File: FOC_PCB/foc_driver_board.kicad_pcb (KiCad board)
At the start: 4 copper layers, 98 x 63.4 mm, 49 parts, among them J1 STM32-Prog-Header, J2 Conn_01x02_Pin, J3 Conn_01x06_Pin, J4 Conn_01x18, J5 Conn_01x02_Pin, SW1 SW_Push, U2 AZ1117IH-3.3, U3 AZ1117IH-5.0, U4 MCP2542FD, U5 STM32G491KEUx, U6 MCP6007, X1 OXETDLJANF-8MHZ

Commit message: Refactor PCB layout
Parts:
- removed C9: 0u1, Capacitor_SMD:C_0603_1608Metric
- removed J5: Conn_01x02_Pin, Connector_PinSocket_2.54mm:PinSocket_1x02_P2.54mm_Vertical
- removed R2: 10k, Resistor_SMD:R_0603_1608Metric
- removed SW1: SW_Push, Button_Switch_THT:SW_PUSH_6mm
- removed U5: STM32G491KEUx, Package_DFN_QFN:QFN-32-1EP_5x5mm_P0.5mm_EP3.45x3.45mm
- added C20: 0u1, Capacitor_SMD:C_0603_1608Metric_Pad1.08x0.95mm_HandSolder, B.Cu at (166.5, 88.5)
- added C21: 0u1, Capacitor_SMD:C_0603_1608Metric_Pad1.08x0.95mm_HandSolder, B.Cu at (165.5, 92.1)
- added C22: 0u1, Capacitor_SMD:C_0603_1608Metric_Pad1.08x0.95mm_HandSolder, B.Cu at (161.0, 92.1)
- added C23: 1u, Capacitor_SMD:C_0603_1608Metric_Pad1.08x0.95mm_HandSolder, B.Cu at (162.5, 92.1)
- added C24: 0u1, Capacitor_SMD:C_0603_1608Metric_Pad1.08x0.95mm_HandSolder, F.Cu at (194.0, 92.5)
- added C25: 0u1, Capacitor_SMD:C_0603_1608Metric_Pad1.08x0.95mm_HandSolder, F.Cu at (194.0, 89.0)
- added C28: 0u1, Capacitor_SMD:C_0603_1608Metric_Pad1.08x0.95mm_HandSolder, B.Cu at (162.2, 78.0)
- added C29: 0u1, Capacitor_SMD:C_0603_1608Metric_Pad1.08x0.95mm_HandSolder, B.Cu at (172.0, 78.0)
- added C30: 0u1, Capacitor_SMD:C_0603_1608Metric_Pad1.08x0.95mm_HandSolder, B.Cu at (179.2, 78.0)
- added D2: LED, LED_SMD:LED_0805_2012Metric_Pad1.15x1.40mm_HandSolder, B.Cu at (148.5, 109.0)
- added D3: LED, LED_SMD:LED_0805_2012Metric_Pad1.15x1.40mm_HandSolder, B.Cu at (203.0, 109.5)
- added J6: Conn_01x02_Pin, Connector_PinSocket_2.54mm:PinSocket_1x02_P2.54mm_Vertical, B.Cu at (170.5, 75.0)
- added J7: Conn_01x02_Pin, Connector_PinSocket_2.54mm:PinSocket_1x02_P2.54mm_Vertical, B.Cu at (178.0, 75.0)
- added Q1: BSS138, Package_TO_SOT_SMD:SOT-23, B.Cu at (164.5, 64.0)
- added R5: 10k, Resistor_SMD:R_0603_1608Metric_Pad0.98x0.95mm_HandSolder, B.Cu at (167.5, 64.0)
- added R6: 10k, Resistor_SMD:R_0603_1608Metric_Pad0.98x0.95mm_HandSolder, B.Cu at (161.5, 65.0)
- added R7: 10k, Resistor_SMD:R_0603_1608Metric_Pad0.98x0.95mm_HandSolder, B.Cu at (184.8, 98.0)
- added R8: 10k, Resistor_SMD:R_0603_1608Metric_Pad0.98x0.95mm_HandSolder, B.Cu at (184.0, 95.5)
- added R9: 10k, Resistor_SMD:R_0603_1608Metric_Pad0.98x0.95mm_HandSolder, B.Cu at (183.0, 89.5)
- added SW2: SW_Push, Button_Switch_THT:SW_PUSH_6mm, F.Cu at (185.5, 102.5)
- added U1: STM32G491RET6, Package_QFP:LQFP-64_10x10mm_P0.5mm, B.Cu at (173.7, 93.8)
- C1, C5: value 22u -> 10u; footprint Capacitor_SMD:C_0603_1608Metric -> Capacitor_SMD:C_0805_2012Metric_Pad1.18x1.45mm_HandSolder
- C10, C11, C13, C14, C15, C16, C17, C18, C19, C2, C6, C8: footprint Capacitor_SMD:C_0603_1608Metric -> Capacitor_SMD:C_0603_1608Metric_Pad1.08x0.95mm_HandSolder
- C12: value 10n -> 0u1; footprint Capacitor_SMD:C_0603_1608Metric -> Capacitor_SMD:C_0603_1608Metric_Pad1.08x0.95mm_HandSolder; moved to F.Cu
- C3, C7: footprint Capacitor_SMD:C_0603_1608Metric -> Capacitor_SMD:C_0805_2012Metric_Pad1.18x1.45mm_HandSolder
- C4: footprint Capacitor_SMD:C_0603_1608Metric -> Capacitor_SMD:C_0603_1608Metric_Pad1.08x0.95mm_HandSolder; moved to B.Cu
- J4: value Conn_01x18 -> ST7796 DIsplay
- R1: footprint Resistor_SMD:R_0603_1608Metric -> Resistor_SMD:R_0603_1608Metric_Pad0.98x0.95mm_HandSolder; moved to B.Cu
- R3, R4: value 10k -> 4k7; footprint Resistor_SMD:R_0603_1608Metric -> Resistor_SMD:R_0603_1608Metric_Pad0.98x0.95mm_HandSolder
- U4: moved to B.Cu
- U6: value MCP6007 -> LSM6DSO32TR; footprint Package_SO:SOIC-8_3.9x4.9mm_P1.27mm -> FOC_Custom_Library:LGA-14L_2P5X3X0P83_STM; moved to F.Cu
- X1: value OXETDLJANF-8MHZ -> OXETDLJANF-8MHZ
- moved R4 62.7 mm to (204.5, 106.2), turned to -90 degrees
- moved R3 42.4 mm to (150.5, 109.0), turned to -90 degrees
- moved U6 37.9 mm to (191.0, 91.0), turned to 90 degrees
- moved kibuzzard-678986CF 37.6 mm to (212.0, 78.8)
- moved G*** 33.4 mm to (142.2, 80.2)
- moved C14 31.1 mm to (168.5, 101.0), turned to -45 degrees
- moved C12 26.0 mm to (183.2, 111.5), turned to 0 degrees
- moved G*** 25.8 mm to (132.2, 98.8)
- moved J2 18.5 mm to (163.5, 75.0)
- moved C11 15.1 mm to (165.5, 87.5), turned to -135 degrees
- moved C4 14.8 mm to (195.0, 79.0)
- moved C3 11.5 mm to (202.0, 106.2), turned to -90 degrees
- moved C1 11.4 mm to (196.8, 112.0), turned to 0 degrees
- moved R1 11.0 mm to (194.5, 81.7), turned to -90 degrees
- moved U4 10.8 mm to (189.5, 81.5)
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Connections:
- net /CAN_N renamed /foc_driver_board/CAN_N
- net /CAN_P renamed /foc_driver_board/CAN_P
- net /DIN2 renamed /foc_driver_board/DIN2
- net /DIN3 renamed /foc_driver_board/DIN3
- net /DIN4 renamed /foc_driver_board/DIN4
- net /DIN5 renamed /foc_driver_board/DIN5
- net /SPI_MISO renamed SPI_MISO
- net /SPI_MOSI renamed SPI_MOSI
- net /SPI_SCK renamed SPI_SCK
- net /SWCLK renamed SWCLK
- net /SWDIO renamed SWDIO
- net VCC renamed +7V
- C10 pad 1: +3.3V -> +3V3
- C11 pad 1: +3.3V -> +3V3
- C12 pad 1: +3.3VA -> NRST
- C14 pad 1: +5V -> +3V3
- C2 pad 1: +3.3V -> +3V3
- C3 pad 1: +3.3V -> +3V3
- C4 pad 1: +3.3V -> +3V3
- C8 pad 1: +3.3V -> +3V3
- FB1 pad 1: +3.3V -> +3V3
- J1 pad 1: unconnected-(J1-RST-Pad1) -> NRST
- J1 pad 10: unconnected-(J1-5V-Pad10) -> +5V
- J1 pad 3: unconnected-(J1-SWIM-Pad3) -> SWO
- J1 pad 7: +3.3V -> +3V3
- J1 pad 8: +3.3V -> +3V3
- J1 pad 9: unconnected-(J1-5V-Pad9) -> +5V
- J2 pad 1: /PB3 -> BTN1
- J4 pad 11: /T_CS -> T_CS
- J4 pad 14: /T_IRQ -> T_IRQ
- J4 pad 15: unconnected-(J4-Pin_15-Pad15) -> (no net)
- J4 pad 16: unconnected-(J4-Pin_16-Pad16) -> (no net)
- J4 pad 17: unconnected-(J4-Pin_17-Pad17) -> (no net)
- J4 pad 18: unconnected-(J4-Pin_18-Pad18) -> (no net)
- J4 pad 3: /LCD_CS -> LCD_CS
- J4 pad 4: /LCD_RESET -> LCD_RESET
- J4 pad 5: /LCD_DC/RS -> LCD_DC
- J4 pad 8: /LCD_BRIGHT -> LCD_BRIGHT
- LED1 pad 4: /DIN1 -> /foc_driver_board/DIN1
- R3 pad 1: +3.3V -> +5V
- R3 pad 2: Net-(U6A--) -> /foc_driver_board/5V_LED
- R4 pad 1: Net-(U6A--) -> +3V3
- R4 pad 2: GNDA -> /foc_driver_board/3V3_LED
- U2 pad 2: +3.3V -> +3V3
- U4 pad 1: /FDCAN_TX -> FDCAN_TX
- U4 pad 4: /FDCAN_RX -> FDCAN_RX
- U4 pad 5: +3.3V -> +3V3
- U4 pad 8: /FDCAN_STBY -> FDCAN_STBY
- U6 pad 1: /DIN1 -> IMU_SA0
- U6 pad 2: Net-(U6A--) -> +3V3
- U6 pad 3: /LED_{SET} -> +3V3
- U6 pad 4: GNDA -> IMU_INT1
- U6 pad 5: unconnected-(U6B-+-Pad5) -> +3V3
- U6 pad 6: unconnected-(U6B---Pad6) -> GNDA
- U6 pad 7: unconnected-(U6-Pad7) -> GNDA
- U6 pad 8: +5V -> +3V3
- X1 pad 1: +3.3V -> +3V3
- X1 pad 3: /RCC -> RCC
- X1 pad 4: +3.3V -> +3V3
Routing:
- net +3.3V: track 184.8 -> 0.00 mm, vias 8 -> 0
- net +5V: track 153.5 -> 0.00 mm, vias 4 -> 0
- net SPI_MISO: track 88.0 -> 0.00 mm, vias 4 -> 0
- net SPI_MOSI: track 85.1 -> 0.00 mm, vias 3 -> 0
- net SPI_SCK: track 81.2 -> 0.00 mm, vias 5 -> 0
- net /T_IRQ: track 78.5 -> 0.00 mm, vias 3 -> 0
- net /T_CS: track 70.7 -> 0.00 mm, vias 3 -> 0
- net GNDA: track 56.1 -> 0.00 mm, vias 342 -> 0
- net /LCD_CS: track 53.9 -> 0.00 mm, vias 3 -> 0
- net /LCD_DC/RS: track 50.1 -> 0.00 mm, vias 3 -> 0
- net /LCD_BRIGHT: track 49.2 -> 0.00 mm, vias 3 -> 0
- net /LCD_RESET: track 48.3 -> 0.00 mm, vias 3 -> 0
- net /LED_{SET}: track 44.1 -> 0.00 mm, vias 2 -> 0
- net SWDIO: track 37.0 -> 0.00 mm, vias 2 -> 0
- net SWCLK: track 36.2 -> 0.00 mm, vias 2 -> 0
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- removed copper zone on B.Cu, net +12V
- removed copper zone on B.Cu, net +7V
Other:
- rule pad_to_mask_clearance: 0 -> 0.05

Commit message: PCB: Finish layout and begin routing
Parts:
- added R10: 10k, Resistor_SMD:R_0603_1608Metric_Pad0.98x0.95mm_HandSolder, B.Cu at (182.2, 79.8)
- added R11: 10k, Resistor_SMD:R_0603_1608Metric_Pad0.98x0.95mm_HandSolder, B.Cu at (172.5, 79.8)
- added R12: 10k, Resistor_SMD:R_0603_1608Metric_Pad0.98x0.95mm_HandSolder, B.Cu at (162.5, 79.8)
- C12, C24, C25, SW2, U6: moved to B.Cu
- C4, C6, D1, R1, U4: moved to F.Cu
- moved Q1 19.3 mm to (161.0, 83.0)
- moved R5 19.3 mm to (164.0, 83.0)
- moved R6 18.6 mm to (157.0, 83.0), turned to 0 degrees
- moved C11 14.9 mm to (167.2, 102.2), turned to -45 degrees
- moved C4 11.2 mm to (186.5, 86.2), turned to -90 degrees
- moved C25 7.45 mm to (198.5, 94.9), turned to 90 degrees
- moved R1 7.28 mm to (190.2, 87.5), turned to 0 degrees
- moved C6 6.52 mm to (190.2, 78.0), turned to 0 degrees
- moved C12 5.20 mm to (179.0, 108.5), turned to 90 degrees
- moved U6 4.92 mm to (195.5, 92.9), turned to -90 degrees
- moved FB1 4.75 mm to (165.4, 87.2), turned to -135 degrees
- moved C24 4.67 mm to (198.5, 91.4), turned to -90 degrees
- moved SW2 4.26 mm to (188.2, 105.8), turned to 180 degrees
- moved J7 3.11 mm to (181.1, 75.0)
- moved C30 2.95 mm to (182.2, 78.0)
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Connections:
- net /foc_driver_board/CAN_N renamed /foc_driver_board/FDCAN-
- net /foc_driver_board/CAN_P renamed /foc_driver_board/FDCAN+
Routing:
- net GNDA: track 0.00 -> 74.3 mm, vias 0 -> 49
- net SPI_MISO: track 0.00 -> 73.9 mm, vias 0 -> 2
- net SPI_MOSI: track 0.00 -> 63.0 mm, vias 0 -> 2
- net +3V3: track 0.00 -> 60.5 mm
- net SPI_SCK: track 0.00 -> 53.4 mm, vias 0 -> 2
- net T_IRQ: track 0.00 -> 52.5 mm
- net T_CS: track 0.00 -> 47.2 mm, vias 0 -> 2
- net LCD_CS: track 0.00 -> 44.5 mm, vias 0 -> 2
- net LCD_RESET: track 0.00 -> 43.6 mm
- net LCD_DC: track 0.00 -> 42.8 mm
- net LCD_BRIGHT: track 0.00 -> 41.7 mm
- net NRST: track 0.00 -> 38.9 mm, vias 0 -> 4
- net /foc_driver_board/FDCAN-: track 0.00 -> 36.5 mm, vias 0 -> 1
- net SWDIO: track 0.00 -> 36.0 mm, vias 0 -> 2
- net /foc_driver_board/FDCAN+: track 0.00 -> 35.7 mm, vias 0 -> 1
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- added copper zone on In2.Cu, net GNDA

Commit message: PCB: Finish routing
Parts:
- moved C15 1.20 mm to (160.2, 69.2)
- moved C16 0.45 mm to (174.0, 69.2)
- moved C18 0.45 mm to (188.0, 69.2)
- moved LED1 0.45 mm to (160.1, 64.7)
- moved LED2 0.45 mm to (167.1, 64.7)
- moved LED3 0.45 mm to (174.1, 64.7)
- moved LED4 0.45 mm to (181.1, 64.7)
- moved LED5 0.45 mm to (188.1, 64.7)
- moved C17 0.45 mm to (181.2, 69.2)
- moved C19 0.45 mm to (167.2, 69.2)
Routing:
- net +3V3: track 60.5 -> 213.3 mm, vias 0 -> 7
- net +5V: track 16.9 -> 152.0 mm, vias 0 -> 3
- net GNDA: track 74.3 -> 128.1 mm, vias 49 -> 53
- net NRST: track 38.9 -> 38.1 mm, vias 4 -> 3
- net /foc_driver_board/FDCAN-: track 36.5 -> 36.7 mm, vias 1 -> 0
- net /foc_driver_board/FDCAN+: vias 1 -> 0
- added copper zone on B.Cu, net +12V
- added copper zone on B.Cu, net +5V
- added copper zone on B.Cu, net +7V
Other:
- rule pad_to_mask_clearance: 0.05 -> 0.025

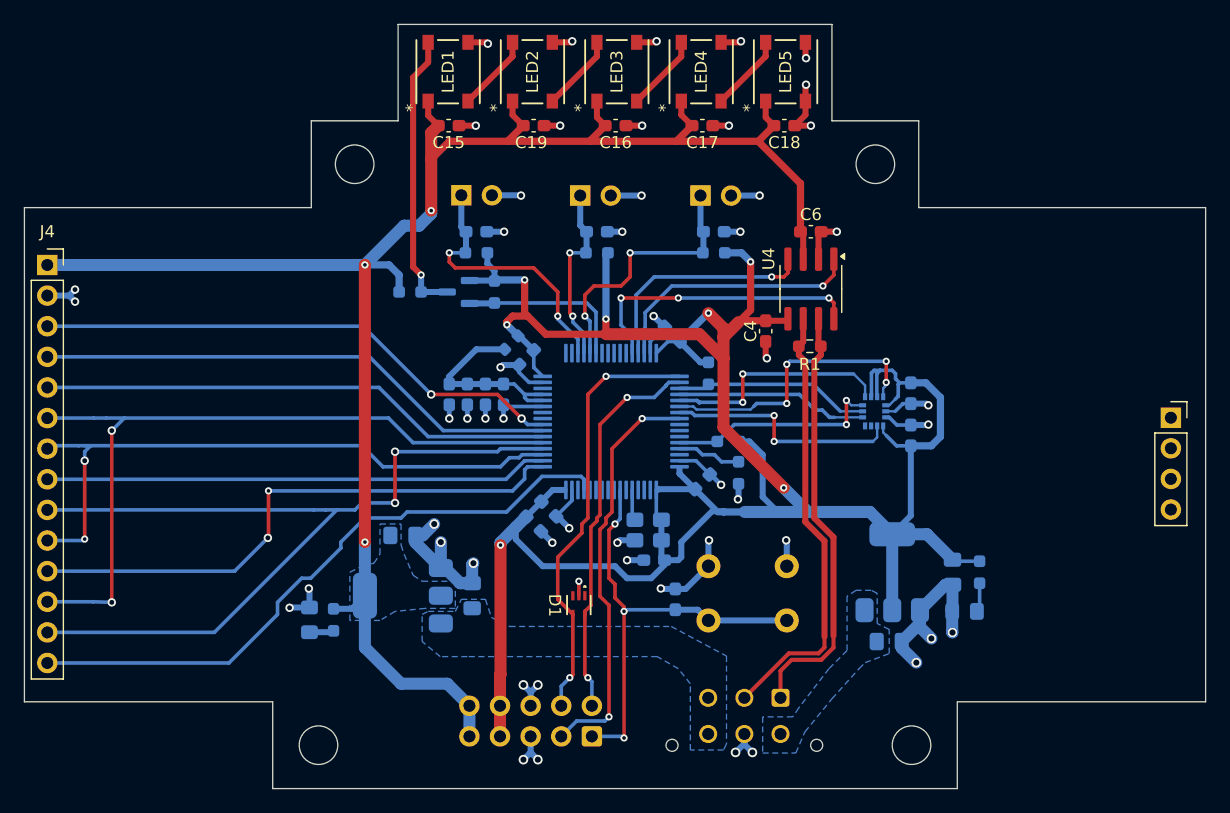
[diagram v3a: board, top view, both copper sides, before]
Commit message: PCB: Add teardrops
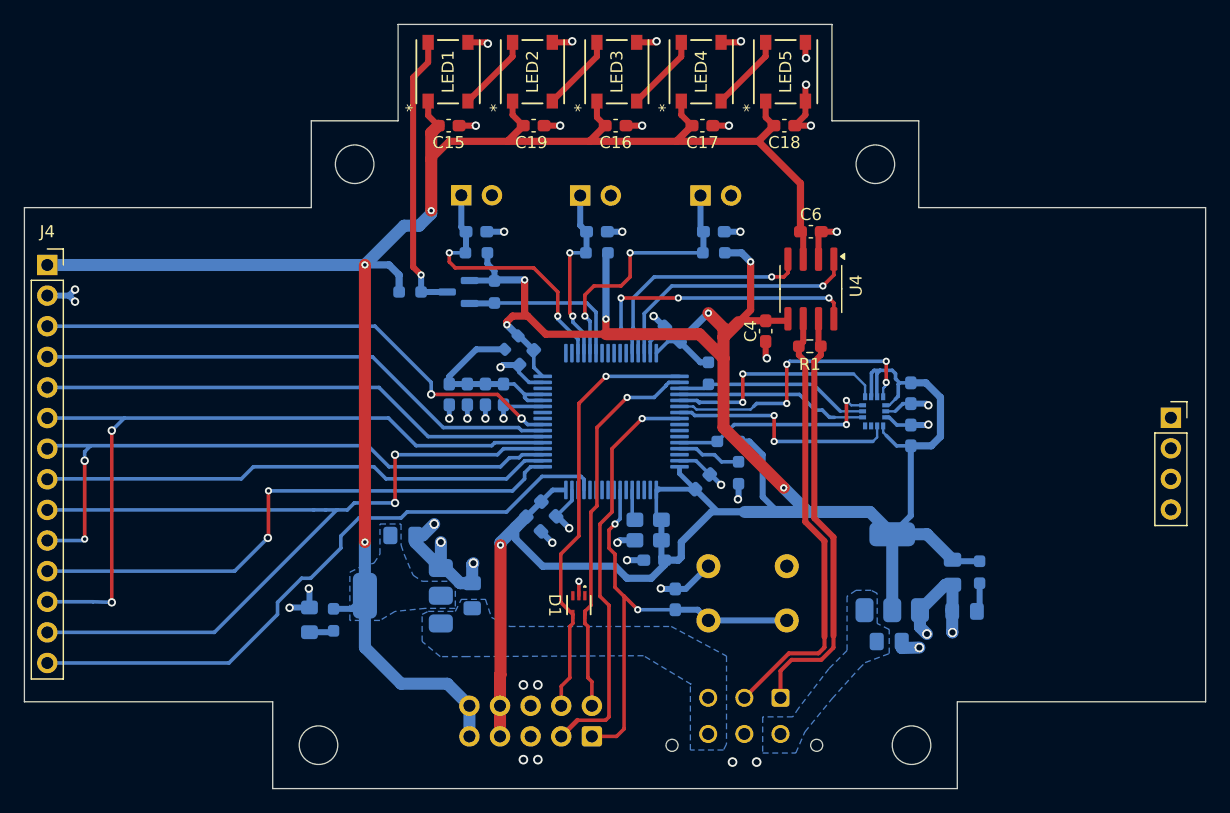
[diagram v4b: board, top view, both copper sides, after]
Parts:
- removed kibuzzard-678986CF: G***, kibuzzard-678986CF
- moved G*** 74.9 mm to (214.2, 98.0), turned to 90 degrees
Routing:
- net GNDA: track 128.1 -> 104.0 mm, vias 53 -> 48
- net LCD_BRIGHT: track 41.7 -> 42.6 mm
- net LCD_CS: track 44.5 -> 45.1 mm
- net SWDIO: track 36.0 -> 35.8 mm, vias 2 -> 1
- net NRST: track 38.1 -> 38.0 mm, vias 3 -> 2
- net SWO: vias 2 -> 1
- net SWCLK: vias 2 -> 1
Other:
- board text added: "Dash Campbell"
